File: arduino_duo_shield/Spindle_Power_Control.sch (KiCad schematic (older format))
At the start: 19 parts, among them J1 Spindle_Power, J7 Power_In, K1 JQC-3F, P14 CONN_01X01, P15 CONN_01X01, P16 CONN_01X01, P17 CONN_01X01, Q1 2N7000, Q2 IRFZ44N, U3 PC817, U5 PC817

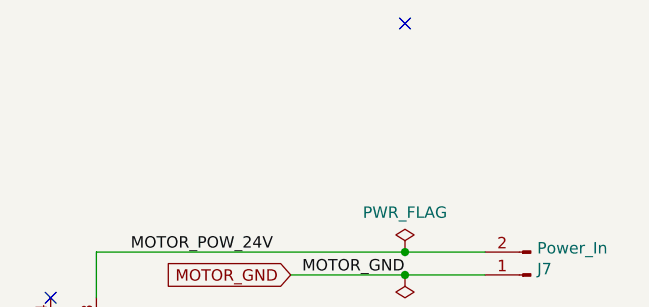
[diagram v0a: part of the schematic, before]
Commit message: Add signal mirror and control jumpers
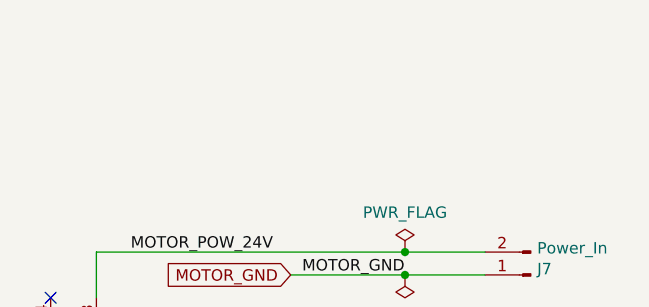
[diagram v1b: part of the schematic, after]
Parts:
- R1, R16, R17, R18, R2: footprint Resistor_THT:R_Axial_DIN0204_L3.6mm_D1.6mm_P5.08mm_Horizontal -> Resistor_THT:R_Axial_DIN0207_L6.3mm_D2.5mm_P7.62mm_Horizontal
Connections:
- no-connect marks 6 -> 5
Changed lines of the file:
@@
 EESchema Schematic File Version 4
-LIBS:arduino_duo_shield-cache
 EELAYER 30 0
 EELAYER END
@@
 F 0 "R1" H 3970 4846 50  0000 L CNN
 F 1 "220" H 3970 4755 50  0000 L CNN
-F 2 "Resistor_THT:R_Axial_DIN0204_L3.6mm_D1.6mm_P5.08mm_Horizontal" V 3830 4800 50  0001 C CNN
+F 2 "Resistor_THT:R_Axial_DIN0207_L6.3mm_D2.5mm_P7.62mm_Horizontal" V 3830 4800 50  0001 C CNN
 F 3 "~" H 3900 4800 50  0001 C CNN
 	1    3900 4800
@@
 F 0 "R2" H 5970 5296 50  0000 L CNN
 F 1 "1.3K" H 5970 5205 50  0000 L CNN
-F 2 "Resistor_THT:R_Axial_DIN0204_L3.6mm_D1.6mm_P5.08mm_Horizontal" V 5830 5250 50  0001 C CNN
+F 2 "Resistor_THT:R_Axial_DIN0207_L6.3mm_D2.5mm_P7.62mm_Horizontal" V 5830 5250 50  0001 C CNN
 F 3 "~" H 5900 5250 50  0001 C CNN
 	1    5900 5250
@@
 F 0 "R16" H 5970 5796 50  0000 L CNN
 F 1 "1K" H 5970 5705 50  0000 L CNN
-F 2 "Resistor_THT:R_Axial_DIN0204_L3.6mm_D1.6mm_P5.08mm_Horizontal" V 5830 5750 50  0001 C CNN
+F 2 "Resistor_THT:R_Axial_DIN0207_L6.3mm_D2.5mm_P7.62mm_Horizontal" V 5830 5750 50  0001 C CNN
 F 3 "~" H 5900 5750 50  0001 C CNN
 	1    5900 5750
@@
 F 0 "R17" H 3970 3596 50  0000 L CNN
 F 1 "100" H 3970 3505 50  0000 L CNN
-F 2 "Resistor_THT:R_Axial_DIN0204_L3.6mm_D1.6mm_P5.08mm_Horizontal" V 3830 3550 50  0001 C CNN
+F 2 "Resistor_THT:R_Axial_DIN0207_L6.3mm_D2.5mm_P7.62mm_Horizontal" V 3830 3550 50  0001 C CNN
 F 3 "~" H 3900 3550 50  0001 C CNN
 	1    3900 3550
@@
 F 0 "R18" H 4770 4196 50  0000 L CNN
 F 1 "10K" H 4770 4105 50  0000 L CNN
-F 2 "Resistor_THT:R_Axial_DIN0204_L3.6mm_D1.6mm_P5.08mm_Horizontal" V 4630 4150 50  0001 C CNN
+F 2 "Resistor_THT:R_Axial_DIN0207_L6.3mm_D2.5mm_P7.62mm_Horizontal" V 4630 4150 50  0001 C CNN
 F 3 "~" H 4700 4150 50  0001 C CNN
 	1    4700 4150
@@
 Wire Wire Line
 	4700 2500 5050 2500
-NoConn ~ 7350 1500
 $EndSCHEMATC
